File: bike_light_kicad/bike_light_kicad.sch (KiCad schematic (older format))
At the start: 54 parts

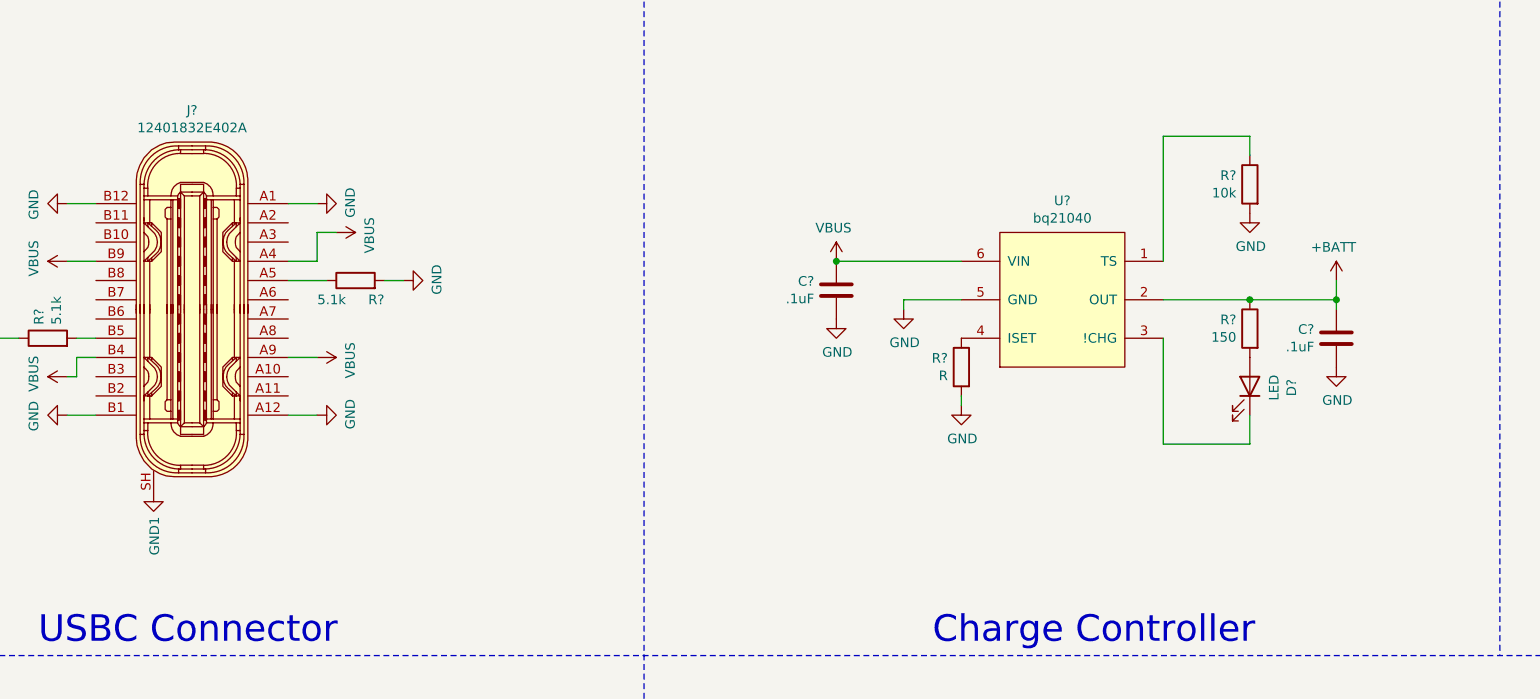
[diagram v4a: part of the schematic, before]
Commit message: charge controller current resistor, ground correction
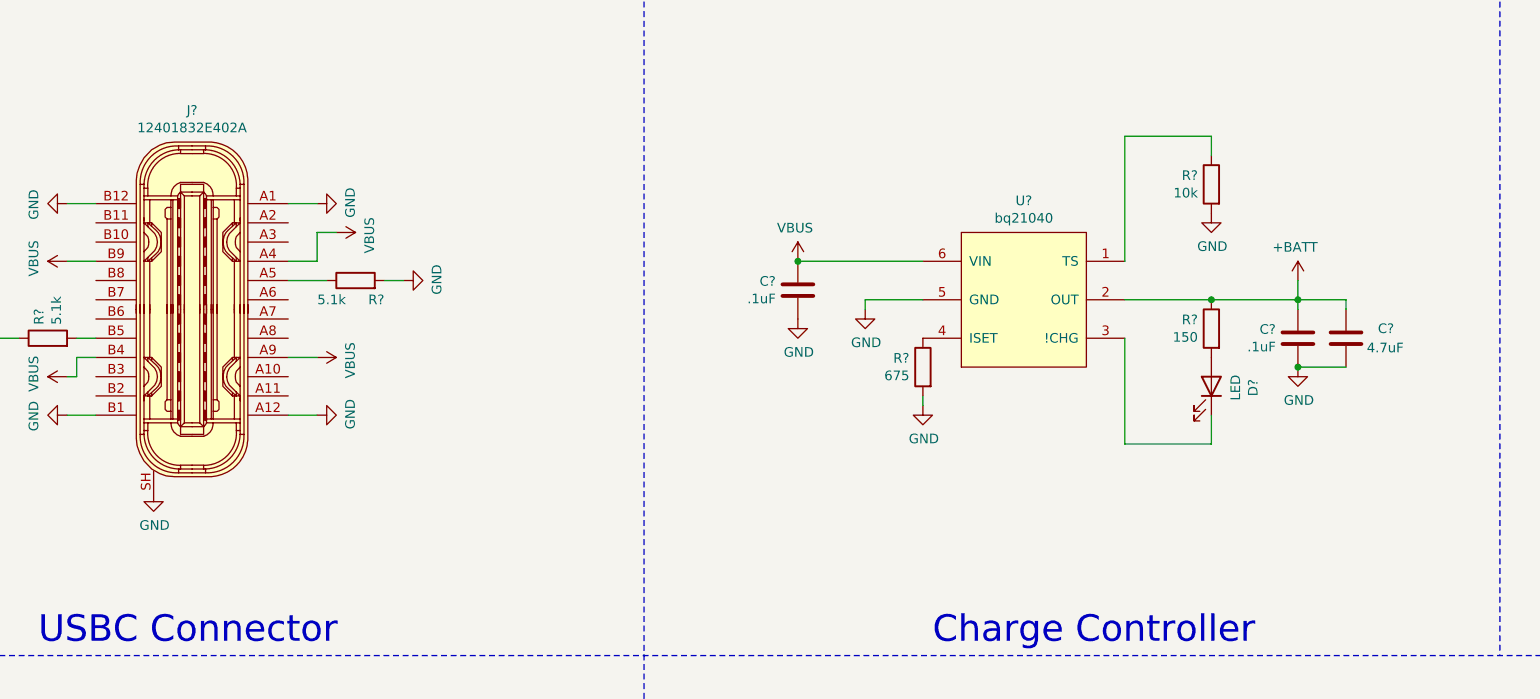
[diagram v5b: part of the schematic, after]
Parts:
- added C?: 4.7uF, symbol Device:C
- R?: value R -> 675
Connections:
- net +BATT: now also C?.1
- net GND: now also J?.SH, C?.2
- net GND1: no longer J?.SH
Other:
- moved on the sheet: C?, D?, R?, U?
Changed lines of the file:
@@
 L Manual_Library:bq21040 U?
 U 1 1 5F54BC79
-P 7150 2600
-F 0 "U?" H 7175 3465 50  0000 C CNN
-F 1 "bq21040" H 7175 3374 50  0000 C CNN
-F 2 "" H 7150 2600 50  0001 C CNN
-F 3 "" H 7150 2600 50  0001 C CNN
-	1    7150 2600
+P 6950 2600
+F 0 "U?" H 6975 3465 50  0000 C CNN
+F 1 "bq21040" H 6975 3374 50  0000 C CNN
+F 2 "" H 6950 2600 50  0001 C CNN
+F 3 "" H 6950 2600 50  0001 C CNN
+	1    6950 2600
 	-1   0    0    -1
 $EndComp
@@
 L Device:C C?
 U 1 1 5F55724B
-P 5950 2200
-F 0 "C?" H 6065 2246 50  0000 L CNN
-F 1 ".1uF" H 6065 2155 50  0000 L CNN
-F 2 "" H 5988 2050 50  0001 C CNN
-F 3 "399-1099-1-ND" H 5950 2200 50  0001 C CNN
-	1    5950 2200
+P 5750 2200
+F 0 "C?" H 5865 2246 50  0000 L CNN
+F 1 ".1uF" H 5865 2155 50  0000 L CNN
+F 2 "" H 5788 2050 50  0001 C CNN
+F 3 "399-1099-1-ND" H 5750 2200 50  0001 C CNN
+	1    5750 2200
 	-1   0    0    -1
 $EndComp
 Wire Wire Line
-	6600 2050 5950 2050
+	6400 2050 5750 2050
 $Comp
 L power:VBUS #PWR?
 U 1 1 5F55F033
-P 5950 2050
-F 0 "#PWR?" H 5950 1900 50  0001 C CNN
-F 1 "VBUS" H 5965 2223 50  0000 C CNN
-F 2 "" H 5950 2050 50  0001 C CNN
-F 3 "" H 5950 2050 50  0001 C CNN
-	1    5950 2050
+P 5750 2050
+F 0 "#PWR?" H 5750 1900 50  0001 C CNN
+F 1 "VBUS" H 5765 2223 50  0000 C CNN
+F 2 "" H 5750 2050 50  0001 C CNN
+F 3 "" H 5750 2050 50  0001 C CNN
+	1    5750 2050
 	-1   0    0    -1
 $EndComp
-Connection ~ 5950 2050
-Wire Wire Line
-	6600 2250 6300 2250
+Connection ~ 5750 2050
+Wire Wire Line
+	6400 2250 6100 2250
 $Comp
 L Device:R R?
 U 1 1 5F56A025
-P 6600 2600
-F 0 "R?" H 6670 2646 50  0000 L CNN
-F 1 "R" H 6670 2555 50  0000 L CNN
-F 2 "" V 6530 2600 50  0001 C CNN
-F 3 "~" H 6600 2600 50  0001 C CNN
-	1    6600 2600
+P 6400 2600
+F 0 "R?" H 6470 2646 50  0000 L CNN
+F 1 "675" H 6470 2555 50  0000 L CNN
+F 2 "" V 6330 2600 50  0001 C CNN
+F 3 "~" H 6400 2600 50  0001 C CNN
+	1    6400 2600
 	-1   0    0    -1
 $EndComp
@@
 L Device:R R?
 U 1 1 5F56BEBA
-P 8100 2400
-F 0 "R?" H 8170 2446 50  0000 L CNN
-F 1 "150" H 8170 2355 50  0000 L CNN
-F 2 "" V 8030 2400 50  0001 C CNN
-F 3 "~" H 8100 2400 50  0001 C CNN
-	1    8100 2400
+P 7900 2400
+F 0 "R?" H 7970 2446 50  0000 L CNN
+F 1 "150" H 7970 2355 50  0000 L CNN
+F 2 "" V 7830 2400 50  0001 C CNN
+F 3 "~" H 7900 2400 50  0001 C CNN
+	1    7900 2400
 	-1   0    0    -1
 $EndComp
@@
 L Device:LED D?
 U 1 1 5F56DF90
-P 8100 2700
-F 0 "D?" H 8093 2917 50  0000 C CNN
-F 1 "LED" H 8093 2826 50  0000 C CNN
-F 2 "" H 8100 2700 50  0001 C CNN
-F 3 "https://optoelectronics.liteon.com/upload/download/DS-22-99-0186/LTST-C190KFKT.PDF" H 8100 2700 50  0001 C CNN
-	1    8100 2700
+P 7900 2700
+F 0 "D?" H 7893 2917 50  0000 C CNN
+F 1 "LED" H 7893 2826 50  0000 C CNN
+F 2 "" H 7900 2700 50  0001 C CNN
+F 3 "https://optoelectronics.liteon.com/upload/download/DS-22-99-0186/LTST-C190KFKT.PDF" H 7900 2700 50  0001 C CNN
+	1    7900 2700
 	0    1    -1   0
 $EndComp
 Wire Wire Line
-	8100 2850 8100 3000
-Wire Wire Line
-	8100 3000 7650 3000
-Wire Wire Line
-	7650 3000 7650 2450
-Wire Wire Line
-	7650 2250 8100 2250
+	7900 2850 7900 3000
+Wire Wire Line
+	7900 3000 7450 3000
+Wire Wire Line
+	7450 3000 7450 2450
+Wire Wire Line
+	7450 2250 7900 2250
 $Comp
 L Device:C C?
 U 1 1 5F57DDA5
-P 8550 2450
-F 0 "C?" H 8665 2496 50  0000 L CNN
-F 1 ".1uF" H 8665 2405 50  0000 L CNN
-F 2 "" H 8588 2300 50  0001 C CNN
-F 3 "399-1099-1-ND" H 8550 2450 50  0001 C CNN
-	1    8550 2450
+P 8350 2450
+F 0 "C?" H 8465 2496 50  0000 L CNN
+F 1 ".1uF" H 8465 2405 50  0000 L CNN
+F 2 "" H 8388 2300 50  0001 C CNN
+F 3 "399-1099-1-ND" H 8350 2450 50  0001 C CNN
+	1    8350 2450
 	-1   0    0    -1
 $EndComp
 Wire Wire Line
-	8100 2250 8550 2250
-Wire Wire Line
-	8550 2250 8550 2300
-Connection ~ 8100 2250
+	7900 2250 8350 2250
+Wire Wire Line
+	8350 2250 8350 2300
+Connection ~ 7900 2250
 $Comp
 L Device:Battery_Cell BT?
@@
 Connection ~ 10800 2000
 Wire Wire Line
-	6600 2800 6600 2750
-Wire Wire Line
-	6300 2300 6300 2250
-Connection ~ 8550 2250
-Wire Wire Line
-	8550 2150 8550 2250
+	6400 2800 6400 2750
+Wire Wire Line
+	6100 2300 6100 2250
+Connection ~ 8350 2250
+Wire Wire Line
+	8350 2150 8350 2250
 $Comp
 L power:+BATT #PWR?
 U 1 1 5F5FEF18
-P 8550 2150
-F 0 "#PWR?" H 8550 2000 50  0001 C CNN
-F 1 "+BATT" H 8565 2323 50  0000 C CNN
-F 2 "" H 8550 2150 50  0001 C CNN
-F 3 "" H 8550 2150 50  0001 C CNN
-	1    8550 2150
+P 8350 2150
+F 0 "#PWR?" H 8350 2000 50  0001 C CNN
+F 1 "+BATT" H 8365 2323 50  0000 C CNN
+F 2 "" H 8350 2150 50  0001 C CNN
+F 3 "" H 8350 2150 50  0001 C CNN
+	1    8350 2150
 	-1   0    0    -1
 $EndComp
@@
 $EndComp
 $Comp
-L power:GND1 #PWR?
-U 1 1 5F4D53A4
-P 2400 3250
-F 0 "#PWR?" H 2400 3000 50  0001 C CNN
-F 1 "GND1" V 2405 3122 50  0000 R CNN
-F 2 "" H 2400 3250 50  0001 C CNN
-F 3 "" H 2400 3250 50  0001 C CNN
-	1    2400 3250
-	1    0    0    -1
-$EndComp
-$Comp
 L Device:R R?
 U 1 1 5F4D8FB6
-P 8100 1650
-F 0 "R?" H 8170 1696 50  0000 L CNN
-F 1 "10k" H 8170 1605 50  0000 L CNN
-F 2 "" V 8030 1650 50  0001 C CNN
-F 3 "~" H 8100 1650 50  0001 C CNN
-	1    8100 1650
+P 7900 1650
+F 0 "R?" H 7970 1696 50  0000 L CNN
+F 1 "10k" H 7970 1605 50  0000 L CNN
+F 2 "" V 7830 1650 50  0001 C CNN
+F 3 "~" H 7900 1650 50  0001 C CNN
+	1    7900 1650
 	-1   0    0    -1
 $EndComp
 Wire Wire Line
-	7650 2050 7650 1400
-Wire Wire Line
-	7650 1400 8100 1400
-Wire Wire Line
-	8100 1400 8100 1500
+	7450 2050 7450 1400
+Wire Wire Line
+	7450 1400 7900 1400
+Wire Wire Line
+	7900 1400 7900 1500
 $Comp
 L power:+4V #PWR?
@@
 L power:GND #PWR?
 U 1 1 5F50C6C4
-P 8100 1800
-F 0 "#PWR?" H 8100 1550 50  0001 C CNN
-F 1 "GND" H 8105 1627 50  0000 C CNN
-F 2 "" H 8100 1800 50  0001 C CNN
-F 3 "" H 8100 1800 50  0001 C CNN
-	1    8100 1800
+P 7900 1800
+F 0 "#PWR?" H 7900 1550 50  0001 C CNN
+F 1 "GND" H 7905 1627 50  0000 C CNN
+F 2 "" H 7900 1800 50  0001 C CNN
+F 3 "" H 7900 1800 50  0001 C CNN
+	1    7900 1800
 	1    0    0    -1
 $EndComp
@@
 L power:GND #PWR?
 U 1 1 5F50DA37
-P 8550 2600
-F 0 "#PWR?" H 8550 2350 50  0001 C CNN
-F 1 "GND" H 8555 2427 50  0000 C CNN
-F 2 "" H 8550 2600 50  0001 C CNN
-F 3 "" H 8550 2600 50  0001 C CNN
-	1    8550 2600
+P 8350 2600
+F 0 "#PWR?" H 8350 2350 50  0001 C CNN
+F 1 "GND" H 8355 2427 50  0000 C CNN
+F 2 "" H 8350 2600 50  0001 C CNN
+F 3 "" H 8350 2600 50  0001 C CNN
+	1    8350 2600
 	1    0    0    -1
 $EndComp
@@
 L power:GND #PWR?
 U 1 1 5F50DDD0
-P 6600 2800
-F 0 "#PWR?" H 6600 2550 50  0001 C CNN
-F 1 "GND" H 6605 2627 50  0000 C CNN
-F 2 "" H 6600 2800 50  0001 C CNN
-F 3 "" H 6600 2800 50  0001 C CNN
-	1    6600 2800
+P 6400 2800
+F 0 "#PWR?" H 6400 2550 50  0001 C CNN
+F 1 "GND" H 6405 2627 50  0000 C CNN
+F 2 "" H 6400 2800 50  0001 C CNN
+F 3 "" H 6400 2800 50  0001 C CNN
+	1    6400 2800
 	1    0    0    -1
 $EndComp
@@
 L power:GND #PWR?
 U 1 1 5F50E3EF
-P 5950 2350
-F 0 "#PWR?" H 5950 2100 50  0001 C CNN
-F 1 "GND" H 5955 2177 50  0000 C CNN
-F 2 "" H 5950 2350 50  0001 C CNN
-F 3 "" H 5950 2350 50  0001 C CNN
-	1    5950 2350
+P 5750 2350
+F 0 "#PWR?" H 5750 2100 50  0001 C CNN
+F 1 "GND" H 5755 2177 50  0000 C CNN
+F 2 "" H 5750 2350 50  0001 C CNN
+F 3 "" H 5750 2350 50  0001 C CNN
+	1    5750 2350
 	1    0    0    -1
 $EndComp
@@
 L power:GND #PWR?
 U 1 1 5F50E7AA
-P 6300 2300
-F 0 "#PWR?" H 6300 2050 50  0001 C CNN
-F 1 "GND" H 6305 2127 50  0000 C CNN
-F 2 "" H 6300 2300 50  0001 C CNN
-F 3 "" H 6300 2300 50  0001 C CNN
-	1    6300 2300
+P 6100 2300
+F 0 "#PWR?" H 6100 2050 50  0001 C CNN
+F 1 "GND" H 6105 2127 50  0000 C CNN
+F 2 "" H 6100 2300 50  0001 C CNN
+F 3 "" H 6100 2300 50  0001 C CNN
+	1    6100 2300
 	1    0    0    -1
 $EndComp
@@
 	2750 7150 2850 7150
 Connection ~ 2850 7150
+$Comp
+L power:GND #PWR?
+U 1 1 5F68CA62
+P 2400 3250
+F 0 "#PWR?" H 2400 3000 50  0001 C CNN
+F 1 "GND" H 2405 3077 50  0000 C CNN
+F 2 "" H 2400 3250 50  0001 C CNN
+F 3 "" H 2400 3250 50  0001 C CNN
+	1    2400 3250
+	1    0    0    -1
+$EndComp
+$Comp
+L Device:C C?
+U 1 1 5F690B0B
+P 8600 2450
+F 0 "C?" H 8350 2500 50  0000 L CNN
+F 1 "4.7uF" H 8300 2400 50  0000 L CNN
+F 2 "" H 8638 2300 50  0001 C CNN
+F 3 "" H 8600 2450 50  0001 C CNN
+	1    8600 2450
+	-1   0    0    -1
+$EndComp
+Wire Wire Line
+	8600 2600 8350 2600
+Connection ~ 8350 2600
+Wire Wire Line
+	8600 2300 8600 2250
+Wire Wire Line
+	8600 2250 8350 2250
 $EndSCHEMATC

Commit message: added some specific part numbers
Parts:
- removed 2.2k, 5.1M (x2): R, symbol Device:R
- removed C? (x6): .1uF, symbol Device:C
- removed C?: 4.7uF, symbol Device:C
- removed R?: 5.1k, symbol Device:R
- removed R?: 330, symbol Device:R
- removed U?: CSD16406Q3, symbol Manual_Library:CSD16406Q3
- added C1, C10, C12, C14, C18, C3, C9: .1uF, Capacitors_SMD:C_0603, symbol Device:C
- added C4: 4.7uF, Capacitors_SMD:C_0603, symbol Device:C
- added R1: 330, Resistors_SMD:R_0603, symbol Device:R
- added R13, R14: 5.1M, Resistors_SMD:R_0603, symbol Device:R
- added R15: 5.1k, Resistors_SMD:R_0603, symbol Device:R
- added R16: -1, Resistors_SMD:R_0603, symbol Device:R
- added R3: 2.2k, Resistors_SMD:R_0603, symbol Device:R
- added U4: CSD16406Q3, digikey-footprints:TDFN-8-1EP, symbol Manual_Library:CSD16406Q3
- C2: renamed from C?; footprint (none) -> Capacitors_SMD:C_0603; Digi-Key_PN (none) -> 399-1099-1-ND; MPN (none) -> C0603C104M4RACTU
- D1: renamed from D?; Digi-Key_PN (none) -> 160-1434-1-ND; MPN (none) -> LTST-C190KFKT
- R2: renamed from R?; footprint (none) -> Resistors_SMD:R_0603; Digi-Key_PN (none) -> 311-10.0KHRCT-ND; MPN (none) -> RC0603FR-0710KL
- R4: renamed from R?; footprint (none) -> Resistors_SMD:R_0603; Digi-Key_PN (none) -> 311-150HRCT-ND; MPN (none) -> RC0603FR-07150RL
- R5: renamed from R?; footprint (none) -> Resistors_SMD:R_0603; Digi-Key_PN (none) -> 311-5.10KHRCT-ND; MPN (none) -> RC0603FR-075K1L
- R6: renamed from R?; value 675 -> 680; footprint (none) -> Resistors_SMD:R_0603; Digi-Key_PN (none) -> YAG3356CT-ND; MPN (none) -> RT0603FRE07680RL
- U2: renamed from U?; footprint (none) -> digikey-footprints:SOT-23-6; Digi-Key_PN (none) -> 296-47315-1-ND; MPN (none) -> BQ21040DBVR
- U3: renamed from U?; footprint (none) -> digikey-footprints:TDFN-8-1EP; Digi-Key_PN (none) -> 296-24251-1-ND; MPN (none) -> CSD16406Q3
- U5: renamed from U?; Digi-Key_PN (none) -> ATTINY85-20SURCT-ND; MPN (none) -> ATTINY85-20SUR
- gave numbers to parts that had none: 33
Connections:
- net +4V: now also C10.1, C18.1
- net +BATT: now also C3.1, C4.1, R1.1
- net Cout: now also R14.1
- net Dout: now also R13.1, U4.5 (D)
- net GND: now also C10.2, C12.2, C14.2, C18.2, C3.2, C4.2, R14.2, R15.1, R3.2
- net GND1: now also C1.2, R13.2, U4.6 (D), U4.7 (D), U4.8 (D)
- net VD: now also C12.1
- net at U1.5 (BAT): now also C1.1, R1.2
- net at U1.6 (V-): now also R3.1
- net at R7.2, R8.1, U6.6 (VDD)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: now also C14.1
- net at J1.A5: now also R15.2
- net at U3.5 (D), U3.6 (D), U3.7 (D)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: now also U4.1 (S), U4.2 (S), U4.3 (S), U4.4 (G)

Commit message: Johns schematic updates
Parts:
- removed C16, C17: 1uF, symbol Device:C
- removed D4, D5, D6, D7, D8: LED, symbol Device:LED
- removed R12: 1k, symbol Device:R
- removed R8: 300k, symbol Device:R
- removed R9: 100k, symbol Device:R
- added C? (x2): 1uF, Capacitor_SMD:C_0603_1608Metric, symbol Device:C
- added D? (x5): LED, symbol Device:LED
- added R?: 10k, Resistors_SMD:R_0603, symbol Device:R
- added R?: 1k, Resistors_SMD:R_0603, symbol Device:R
- added R?: 100k, Resistors_SMD:R_0603, symbol Device:R
- added R?: 300k, Resistors_SMD:R_0603, symbol Device:R
- C15: footprint (none) -> Capacitor_SMD:C_0603_1608Metric; Digi-Key_PN (none) -> 399-11136-1-ND; MPN (none) -> C0603C105M4RACTU
- C18: footprint Capacitors_SMD:C_0603 -> Capacitor_SMD:C_0603_1608Metric
- D?: renamed from D3; Digi-Key_PN (none) -> 1510-2183-1-ND; MPN (none) -> SPMWHT541ML5XATMS6
- J1: symbol Digikey_USB_CON:12401832E402A -> bike_light_kicad-rescue:12401832E402A-Digikey_USB_CON
- J2: footprint (none) -> Connector_PinSocket_2.54mm:PinSocket_2x03_P2.54mm_Vertical; symbol Connector:AVR-ISP-6 -> bike_light_kicad-rescue:AVR-ISP-6-Connector
- U1: value BQ297xy -> BQ29700; Digi-Key_PN (none) -> 296-43985-1-ND; MPN (none) -> BQ29700DSER
- U2: symbol Manual_Library:bq21040 -> bike_light_kicad-rescue:bq21040-Manual_Library
- U3, U4: symbol Manual_Library:CSD16406Q3 -> bike_light_kicad-rescue:CSD16406Q3-Manual_Library
- U5: symbol MCU_Microchip_ATtiny:ATtiny85-20SU -> bike_light_kicad-rescue:ATtiny85-20SU-MCU_Microchip_ATtiny
- U6: footprint (none) -> Package_SO:VSSOP-8_3.0x3.0mm_P0.65mm; symbol Manual_Library:LM2621 -> bike_light_kicad-rescue:LM2621-Manual_Library; Digi-Key_PN (none) -> LM2621MMX/NOPBCT-ND; MPN (none) -> LM2621MMX/NOPB
- U7: symbol Digikey_PMIC_LED:TLC59711PWPR -> bike_light_kicad-rescue:TLC59711PWPR-Digikey_PMIC_LED
- U8: footprint (none) -> Package_TO_SOT_SMD:SOT-23-5; symbol Manual_Library:NCP699SN33T1G -> bike_light_kicad-rescue:NCP699SN33T1G-Manual_Library; Digi-Key_PN (none) -> NCP699SN33T1GOSCT-ND; MPN (none) -> NCP699SN33T1G
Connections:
- net +3V3: now also C?.1, R?.1, R?.1
- net +4V: now also C?.1, D?.2 (A), D?.2 (A), D?.2 (A), D?.2 (A), D?.2 (A)
- net B_IN: now also R?.2
- net CLK: now also U7.10 (SCKI); no longer U7.9 (SDTI)
- net DATA: now also U7.9 (SDTI); no longer U7.10 (SCKI)
- net GND: now also C?.2, C?.2, R?.2
- net at U7.1 (IREF): now also R?.1
- net at U7.13 (OUTR2), U7.16 (OUTR3): now also D?.1 (K)
- net at U7.14 (OUTG2), U7.17 (OUTG3): now also D?.1 (K)
- net at U7.15 (OUTB2), U7.18 (OUTB3): now also D?.1 (K)
- net at U7.3 (OUTR0), U7.6 (OUTR1): now also D?.1 (K)
- net at U7.4 (OUTG0), U7.7 (OUTG1): now also D?.1 (K)
- net at C14.1, R7.2, U6.6 (VDD)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: now also R?.1
- net at U6.3 (FREQ): now also R?.2
- net at J2.5 (~RST), U5.1 (~RESET~/PB5): now also R?.2
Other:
- moved on the sheet: R6

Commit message: added components in standard formatt to smps stage
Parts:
- removed C11, C6, C7, C8: 22uF, symbol Device:C
- removed C13: 39pF, symbol Device:C
- removed C5: 4.7u, symbol Device:C
- removed L2: 22u, symbol Device:L
- removed R10: 150k, symbol Device:R
- removed R11: 67.4k, symbol Device:R
- removed R7: 500, symbol Device:R
- added C? (x4): 22uF, Capacitors_SMD:C_0805, symbol Device:C
- added C?: 4.7uF, Capacitors_SMD:C_1206, symbol Device:C
- added C?: 39pF, Capacitors_SMD:C_0603, symbol Device:C
- added L?: 22u, symbol Device:L
- added R?: 499, Resistors_SMD:R_0603, symbol Device:R
- added R?: 68k, Resistors_SMD:R_0603, symbol Device:R
- added R?: 150k, Resistors_SMD:R_0603, symbol Device:R
- D2: footprint (none) -> Diodes_SMD:D_SOD-323F; Digi-Key_PN (none) -> 1727-3861-2-ND; MPN (none) -> PMEG2015EJ,115
- J1: symbol bike_light_kicad-rescue:12401832E402A-Digikey_USB_CON -> bike_light_kicad-rescue:12401832E402A-Digikey_USB_CON-bike_light_kicad-rescue
- J2: symbol bike_light_kicad-rescue:AVR-ISP-6-Connector -> bike_light_kicad-rescue:AVR-ISP-6-Connector-bike_light_kicad-rescue
- L1: Digi-Key_PN (none) -> SRU1038-220YCT-ND; MPN (none) -> SRU1038-220Y
- U2: symbol bike_light_kicad-rescue:bq21040-Manual_Library -> bike_light_kicad-rescue:bq21040-Manual_Library-bike_light_kicad-rescue
- U3, U4: symbol bike_light_kicad-rescue:CSD16406Q3-Manual_Library -> bike_light_kicad-rescue:CSD16406Q3-Manual_Library-bike_light_kicad-rescue
- U5: symbol bike_light_kicad-rescue:ATtiny85-20SU-MCU_Microchip_ATtiny -> bike_light_kicad-rescue:ATtiny85-20SU-MCU_Microchip_ATtiny-bike_light_kicad-rescue
- U6: symbol bike_light_kicad-rescue:LM2621-Manual_Library -> bike_light_kicad-rescue:LM2621-Manual_Library-bike_light_kicad-rescue
- U7: symbol bike_light_kicad-rescue:TLC59711PWPR-Digikey_PMIC_LED -> bike_light_kicad-rescue:TLC59711PWPR-Digikey_PMIC_LED-bike_light_kicad-rescue
- U8: symbol bike_light_kicad-rescue:NCP699SN33T1G-Manual_Library -> bike_light_kicad-rescue:NCP699SN33T1G-Manual_Library-bike_light_kicad-rescue
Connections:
- net +4V: now also C?.1, C?.1, C?.1, C?.1, R?.1
- net GND: now also C?.2, C?.2, C?.2, C?.2, L?.2, R?.1; no longer L1.2
- net VD: now also L1.1, C?.1, R?.2
- net at D2.2 (A): now also C?.2, L?.1; no longer L1.1
- net at C14.1, R?.1, U6.6 (VDD)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: now also R?.1
- net at U6.8 (SW): now also L1.2, C?.1
- net at U6.4 (FB): now also C?.2, R?.2, R?.2
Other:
- moved on the sheet: L1
